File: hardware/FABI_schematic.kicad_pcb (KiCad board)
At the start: 2 copper layers, 81 x 55 mm, 73 parts, among them J1 Conn_01x02_Pin, J11 009159005551906, J11_GND1 Conn_01x01_Male, J11_VDD1 Conn_01x01_Male, J11_data1 Conn_01x01_Male, J12 Conn_01x04_Socket, J2 display_connector_91601-304LF, J3 54601-906WPLF, J4 54-00174 / FC68125, J5 54-00174 / FC68125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

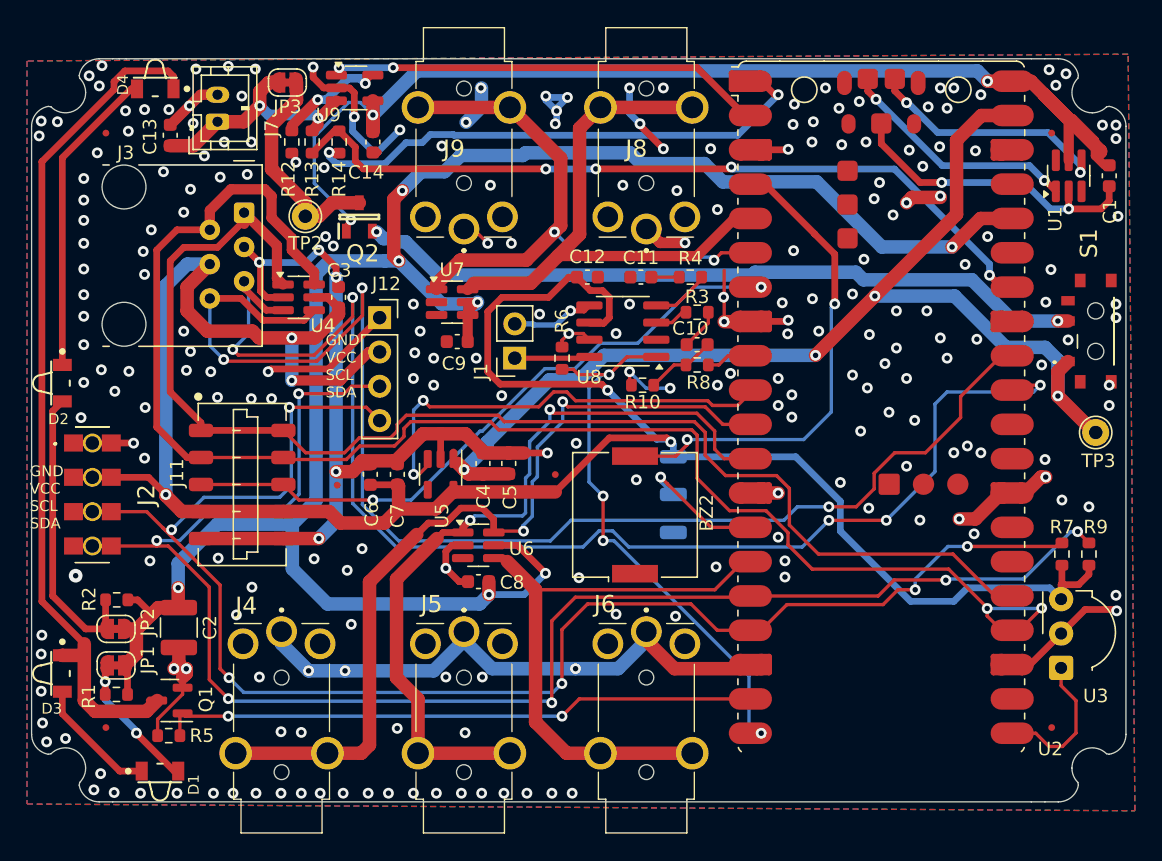
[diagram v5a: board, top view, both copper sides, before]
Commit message: Resetted to prior to commit 61a2890 (FW change) and readded HW changes/commits:
Added Battery Bed + Hole for Power Switch

Adjusted routing to improve ground/copper area coverage

Added 3D Models (54601-906WPLFc.stp, PKMCS0909E4000-R1--3DModel-STEP-56544.STEP)
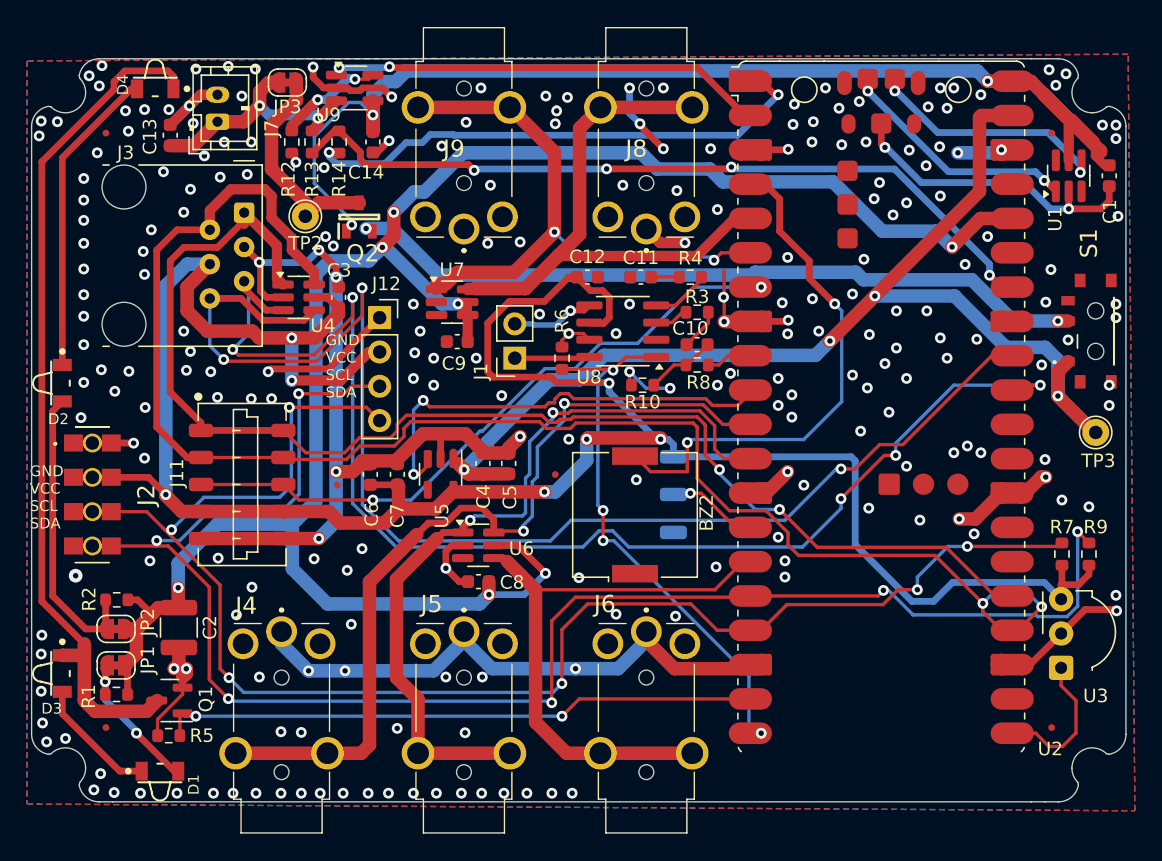
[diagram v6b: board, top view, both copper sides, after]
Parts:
- U2: value SC0918 (PicoW) -> Pico 2W
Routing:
- net GND: track 212.4 -> 199.2 mm
- net /SDA_INT: track 120.6 -> 125.6 mm
- net /NEOPIXEL: track 10.7 -> 7.58 mm
- net +3.3VADC: track 177.7 -> 180.3 mm, vias 5 -> 7
- net /BUZZER: track 35.5 -> 37.9 mm
- net VCC: track 147.6 -> 145.4 mm
- net /EXT1: track 100.4 -> 98.4 mm
- net /SDA: track 114.3 -> 115.8 mm
- net /EXT2: track 99.1 -> 97.6 mm
- net V_PWR_SWITCH: track 54.4 -> 55.5 mm
- net VBUS: track 86.4 -> 87.4 mm
- net /SCL: track 97.6 -> 96.9 mm, vias 0 -> 2
